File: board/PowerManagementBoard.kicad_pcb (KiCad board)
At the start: 2 copper layers, 167.9 x 115.3 mm, 162 parts, among them IC1 ACS37010LLZATR-030B3, IC2 ACS37010LLZATR-030B3, IC3 ACS37010LLZATR-030B3, IC4 ACS37010LLZATR-030B3, IC6 ACS37010LLZATR-030B3, J1 RJ45_LED_Shielded, J10 768250002, J11 768250002, J12 768250002, J13 768250002, J14 768250002, J15 768250002, J16 768250002, J17 768250002, J18 768250002, J2 SS-73100-082, J3 SS-73100-082, J5 768250002, J6 768250002, J7 768250002, J8 768250002, J9 768250002, Q1 BSS138, Q2 IPB180N10S4-02, Q3 Si4162DY, Q4 IPB180N10S4-02, Q5 Si4162DY, Q6 Si4162DY, Q7 Si4162DY, Q8 Si4162DY, Q9 IPB180N10S4-02, U1 LT1910, U10 ACS72981LLRATR-100U3, U11 LT1910, U12 LT1910, U13 LT1910, U14 LT1910, U15 Teensy4.1_DEV-16771, U16 OKI-78SR-3.3_1.5-W36H-C, U17 OKI-78SR-5_1.5-W36H-C, U19 LT1910, U2 LM5050MK-1_NOPB, U3 LM5050MK-1_NOPB, U4 Opamp_Dual, U5 Opamp_Dual, U6 Opamp_Dual

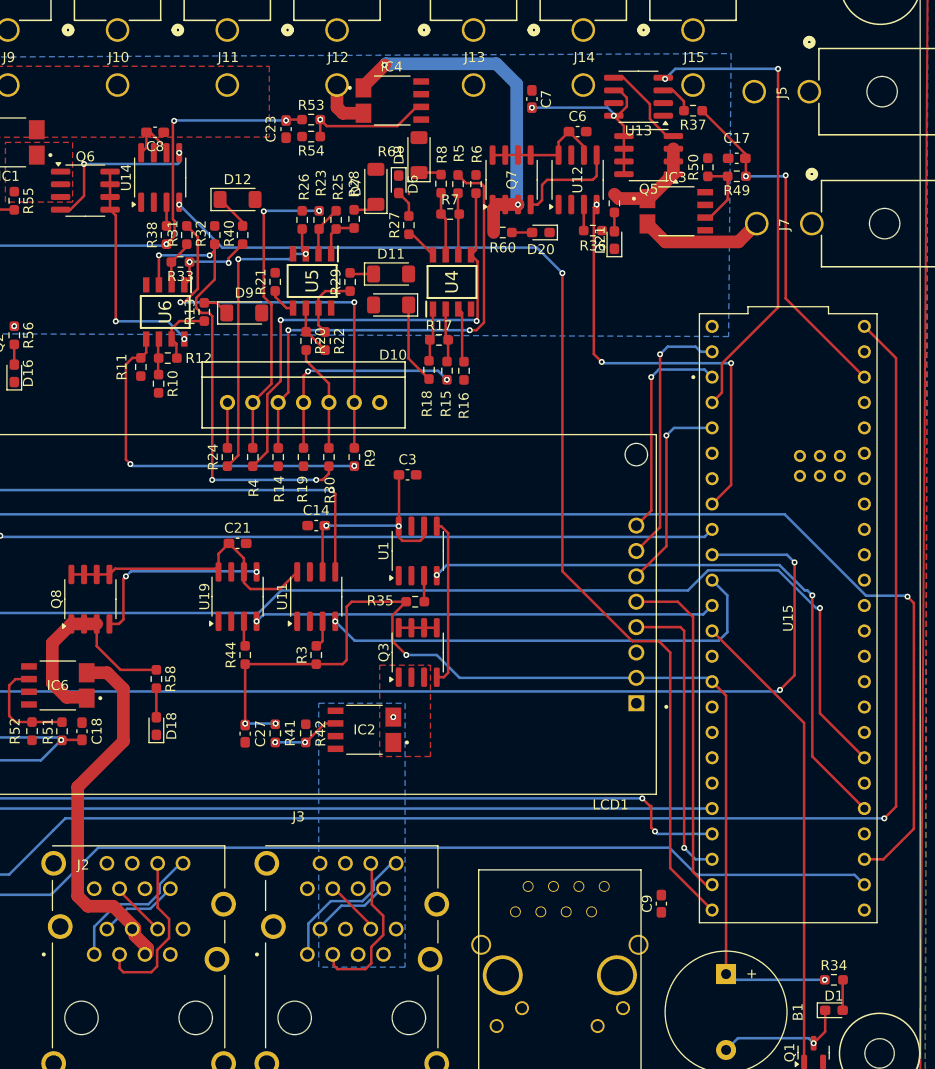
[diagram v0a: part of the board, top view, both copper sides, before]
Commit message: add more traces
seems to be just 24V connections left
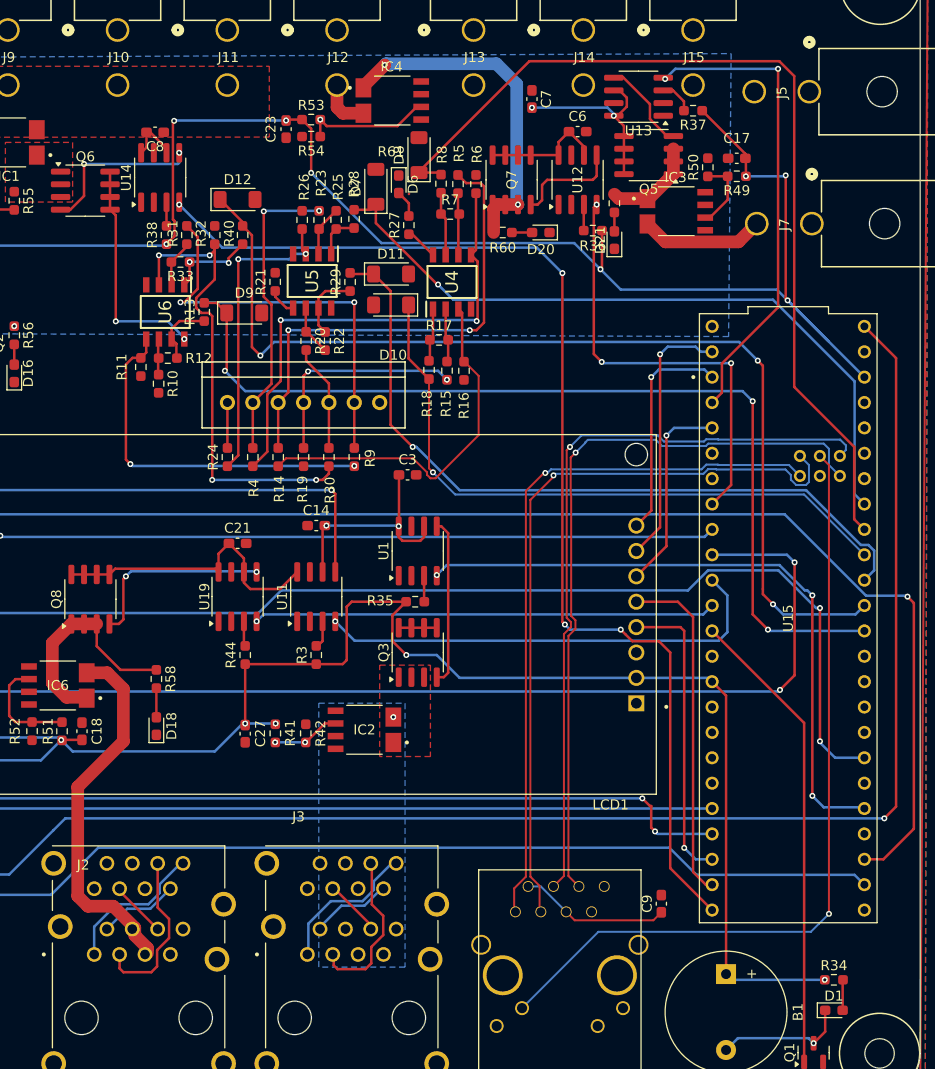
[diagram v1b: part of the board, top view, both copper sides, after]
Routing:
- net /TeensyandEthernetCircuit/CellSense2: track 3.58 -> 103.4 mm, vias 0 -> 3
- net /TeensyandEthernetCircuit/CellSense1: track 2.67 -> 95.8 mm, vias 0 -> 3
- net /TeensyandEthernetCircuit/CellSense5: track 2.29 -> 93.4 mm
- net +3V3: track 340.9 -> 429.4 mm, vias 14 -> 17
- net /TeensyandEthernetCircuit/LED: track 0.00 -> 80.8 mm, vias 0 -> 1
- net /TeensyandEthernetCircuit/RX+: track 0.00 -> 75.0 mm, vias 0 -> 1
- net /TeensyandEthernetCircuit/TX-: track 0.00 -> 74.9 mm, vias 0 -> 1
- net /TeensyandEthernetCircuit/RX-: track 0.00 -> 74.3 mm, vias 0 -> 1
- net /TeensyandEthernetCircuit/CellSense3: track 2.40 -> 75.2 mm, vias 0 -> 1
- net /TeensyandEthernetCircuit/TX+: track 0.00 -> 71.7 mm, vias 0 -> 1
- net /TeensyandEthernetCircuit/CellSense6: track 2.41 -> 71.5 mm, vias 0 -> 1
- net /TeensyandEthernetCircuit/CellSense4: track 8.26 -> 64.4 mm, vias 0 -> 1
- net Net-(U4A-+): track 5.50 -> 36.6 mm
- net Net-(C9-Pad1): track 0.00 -> 15.1 mm
- net /Switching Circuit/LC_EN: track 112.7 -> 115.7 mm, vias 2 -> 4
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
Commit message: Changes before layout review
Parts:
- added D17: GRN, LED_SMD:LED_0603_1608Metric_Pad1.05x0.95mm_HandSolder, F.Cu at (152.8, 109.7)
- added R57: 6.8k, Resistor_SMD:R_0603_1608Metric_Pad0.98x0.95mm_HandSolder, F.Cu at (152.7, 112.3)
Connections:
- net /Current-Sensinator/m5Vout renamed /TeensyandEthernetCircuit/CSensem5
- IC1 pad 7: (no net) -> /Current-Sensinator/LCVout
- IC1 pad 8: (no net) -> +3V3
- IC2 pad 7: (no net) -> /Current-Sensinator/m2Vout
- IC2 pad 8: (no net) -> +3V3
- IC3 pad 7: (no net) -> /Current-Sensinator/NSVout
- IC3 pad 8: (no net) -> +3V3
- IC4 pad 7: (no net) -> /Current-Sensinator/AUXVout
- IC4 pad 8: (no net) -> +3V3
- IC6 pad 7: (no net) -> /Current-Sensinator/m9Vout
- IC6 pad 8: (no net) -> +3V3
- U15 pad 36: /Switching Circuit/M5_EN -> unconnected-(U15-CS2-Pad36)
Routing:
- net +24V: track 167.1 -> 358.5 mm, vias 8 -> 17
- net /Current-Sensinator/LCVout: track 0.00 -> 183.2 mm, vias 0 -> 3
- net /Current-Sensinator/m9out: track 37.6 -> 152.8 mm, vias 0 -> 3
- net /Current-Sensinator/AUXVout: track 0.00 -> 87.3 mm, vias 0 -> 4
- net /Current-Sensinator/m9Vout: track 0.00 -> 71.1 mm, vias 0 -> 1
- net /Current-Sensinator/NSVout: track 0.00 -> 59.9 mm
- net /Current-Sensinator/m2Vout: track 0.00 -> 54.9 mm, vias 0 -> 1
- net +3V3: track 429.4 -> 475.6 mm, vias 17 -> 19
- net /Current-Sensinator/m2out: track 0.00 -> 25.1 mm
- net Net-(U5B-+): track 2.84 -> 19.2 mm
- net GND: track 0.07 -> 9.45 mm
- net Net-(D17-A): track 0.00 -> 2.55 mm
- net /Current-Sensinator/m9in: track 22.7 -> 21.6 mm
- net Net-(U4A-+): track 36.6 -> 36.8 mm, vias 0 -> 2
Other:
- board size 167.9 x 115.3 mm -> 167.6 x 115.1 mm

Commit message: experimented with layout
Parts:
- removed the C13 at (75.0, 122.2)
- removed the C4 at (76.2, 97.3)
- removed R41, R42, R43, R46, R49, R50, R51, R52, R53, R54: 10k, Resistor_SMD:R_0603_1608Metric_Pad0.98x0.95mm_HandSolder
- moved J7 100.4 mm to (108.7, 117.7), turned to 0 degrees
- moved J5 98.1 mm to (122.8, 117.7), turned to 0 degrees
- moved D1 88.9 mm to (164.8, 54.4), turned to 180 degrees
- moved D6 88.7 mm to (77.7, 108.2), turned to 180 degrees
- moved Q1 88.7 mm to (164.8, 58.2)
- moved R34 86.4 mm to (161.0, 55.4), turned to 90 degrees
- moved R27 86.1 mm to (77.7, 106.2), turned to 180 degrees
- moved B1 77.8 mm to (177.8, 57.4), turned to 180 degrees
- moved Q5 74.5 mm to (112.0, 93.7)
- moved D21 74.3 mm to (111.3, 105.7)
- moved R61 74.1 mm to (111.3, 101.6)
- moved C17 73.8 mm to (124.1, 97.5), turned to 0 degrees
- moved C7 72.8 mm to (110.2, 97.8), turned to 180 degrees
- moved IC3 72.5 mm to (117.3, 99.6)
- moved U13 70.4 mm to (120.7, 93.7)
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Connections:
- net Net-(D14-K) renamed /Current Protection/Batt_to_CS
- net Net-(D2-K) renamed /Current Protection/Batt2
- net Net-(D4-K) renamed /Current Protection/Batt1
- IC1 pad 6: Net-(IC1-VREF) -> unconnected-(IC1-VREF-Pad6)
- IC2 pad 6: Net-(IC2-VREF) -> unconnected-(IC2-VREF-Pad6)
- IC3 pad 6: Net-(IC3-VREF) -> unconnected-(IC3-VREF-Pad6)
- IC4 pad 6: Net-(IC4-VREF) -> unconnected-(IC4-VREF-Pad6)
- IC6 pad 6: Net-(IC6-VREF) -> unconnected-(IC6-VREF-Pad6)
- R10 pad 1: Net-(U6B--) -> Net-(U6A--)
- R11 pad 1: Net-(U6B-+) -> Net-(U6A-+)
- R12 pad 2: Net-(U6B--) -> Net-(U6A--)
- R14 pad 1: Net-(U4A-+) -> Net-(U5B-+)
- R15 pad 1: Net-(U4A--) -> Net-(U5B--)
- R16 pad 1: Net-(U4A-+) -> Net-(U5B-+)
- R17 pad 2: Net-(U4A--) -> Net-(U5B--)
- R19 pad 1: Net-(U5B-+) -> Net-(U5A-+)
- R20 pad 1: Net-(U5B--) -> Net-(U5A--)
- R21 pad 1: Net-(U5B-+) -> Net-(U5A-+)
- R22 pad 2: Net-(U5B--) -> Net-(U5A--)
- R23 pad 1: Net-(U5A--) -> Net-(U4B--)
- R24 pad 1: Net-(U5A-+) -> Net-(U4B-+)
- R25 pad 2: Net-(U5A--) -> Net-(U4B--)
- R26 pad 1: Net-(U5A-+) -> Net-(U4B-+)
- R30 pad 1: Net-(U6A-+) -> Net-(U6B-+)
- R31 pad 1: Net-(U6A--) -> Net-(U6B--)
- R32 pad 1: Net-(U6A-+) -> Net-(U6B-+)
- R33 pad 2: Net-(U6A--) -> Net-(U6B--)
- R4 pad 1: Net-(U4B-+) -> Net-(U4A-+)
- R5 pad 1: Net-(U4B--) -> Net-(U4A--)
- R6 pad 1: Net-(U4B-+) -> Net-(U4A-+)
- R7 pad 2: Net-(U4B--) -> Net-(U4A--)
- R9 pad 1: Net-(U6B-+) -> Net-(U6A-+)
- U15 pad 10: /Switching Circuit/M9_EN -> unconnected-(U15-CS1-Pad10)
- U15 pad 27: /TeensyandEthernetCircuit/CSensem5 -> unconnected-(U15-A13-Pad27)
- U15 pad 3.3V_1: +3V3 -> unconnected-(U15-3.3V-Pad3.3V_1)
- U15 pad 3.3V_2: +3V3 -> unconnected-(U15-3.3V-Pad3.3V_1)_1
- U15 pad 36: unconnected-(U15-CS2-Pad36) -> /Switching Circuit/M9_EN
- U4 pad 1: Net-(R17-Pad1) -> Net-(R7-Pad1)
- U4 pad 7: Net-(R7-Pad1) -> Net-(R25-Pad1)
- U5 pad 1: Net-(R25-Pad1) -> Net-(R22-Pad1)
- U5 pad 7: Net-(R22-Pad1) -> Net-(R17-Pad1)
- U6 pad 1: Net-(R33-Pad1) -> Net-(R12-Pad1)
- U6 pad 7: Net-(R12-Pad1) -> Net-(R33-Pad1)
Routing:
- net +3V3: track 475.6 -> 0.00 mm, vias 19 -> 0
- net +24V: track 358.5 -> 146.4 mm, vias 17 -> 1
- net +5V: track 183.5 -> 0.00 mm, vias 1 -> 0
- net /Current-Sensinator/LCVout: track 183.2 -> 0.00 mm, vias 3 -> 0
- net /LCD/D6: track 153.2 -> 0.00 mm, vias 1 -> 0
- net /Current-Sensinator/m9out: track 152.8 -> 0.00 mm, vias 3 -> 0
- net /LCD/D7: track 137.8 -> 0.00 mm, vias 1 -> 0
- net /Current Protection/BattVout: track 135.7 -> 0.00 mm, vias 4 -> 0
- net /Switching Circuit/LC_EN: track 115.7 -> 0.00 mm, vias 4 -> 0
- net /LCD/D3: track 111.9 -> 0.00 mm, vias 2 -> 0
- net /TeensyandEthernetCircuit/CellSense2: track 103.4 -> 0.00 mm, vias 3 -> 0
- net /LCD/D2: track 100.0 -> 0.00 mm, vias 2 -> 0
- net /LCD/D5: track 99.4 -> 0.00 mm, vias 3 -> 0
- net /TeensyandEthernetCircuit/CellSense1: track 95.8 -> 0.00 mm, vias 3 -> 0
- net /LCD/D4: track 95.4 -> 0.00 mm, vias 1 -> 0
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- added copper zone on B.Cu, net +24V
- added copper zone on F.Cu, net /Anderson/AUX
- removed copper zone on F.Cu, net /Current-Sensinator/m2in
- removed copper zone on B.Cu, net /Current-Sensinator/m2out
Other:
- board size 167.6 x 115.1 mm -> 162.3 x 99.6 mm

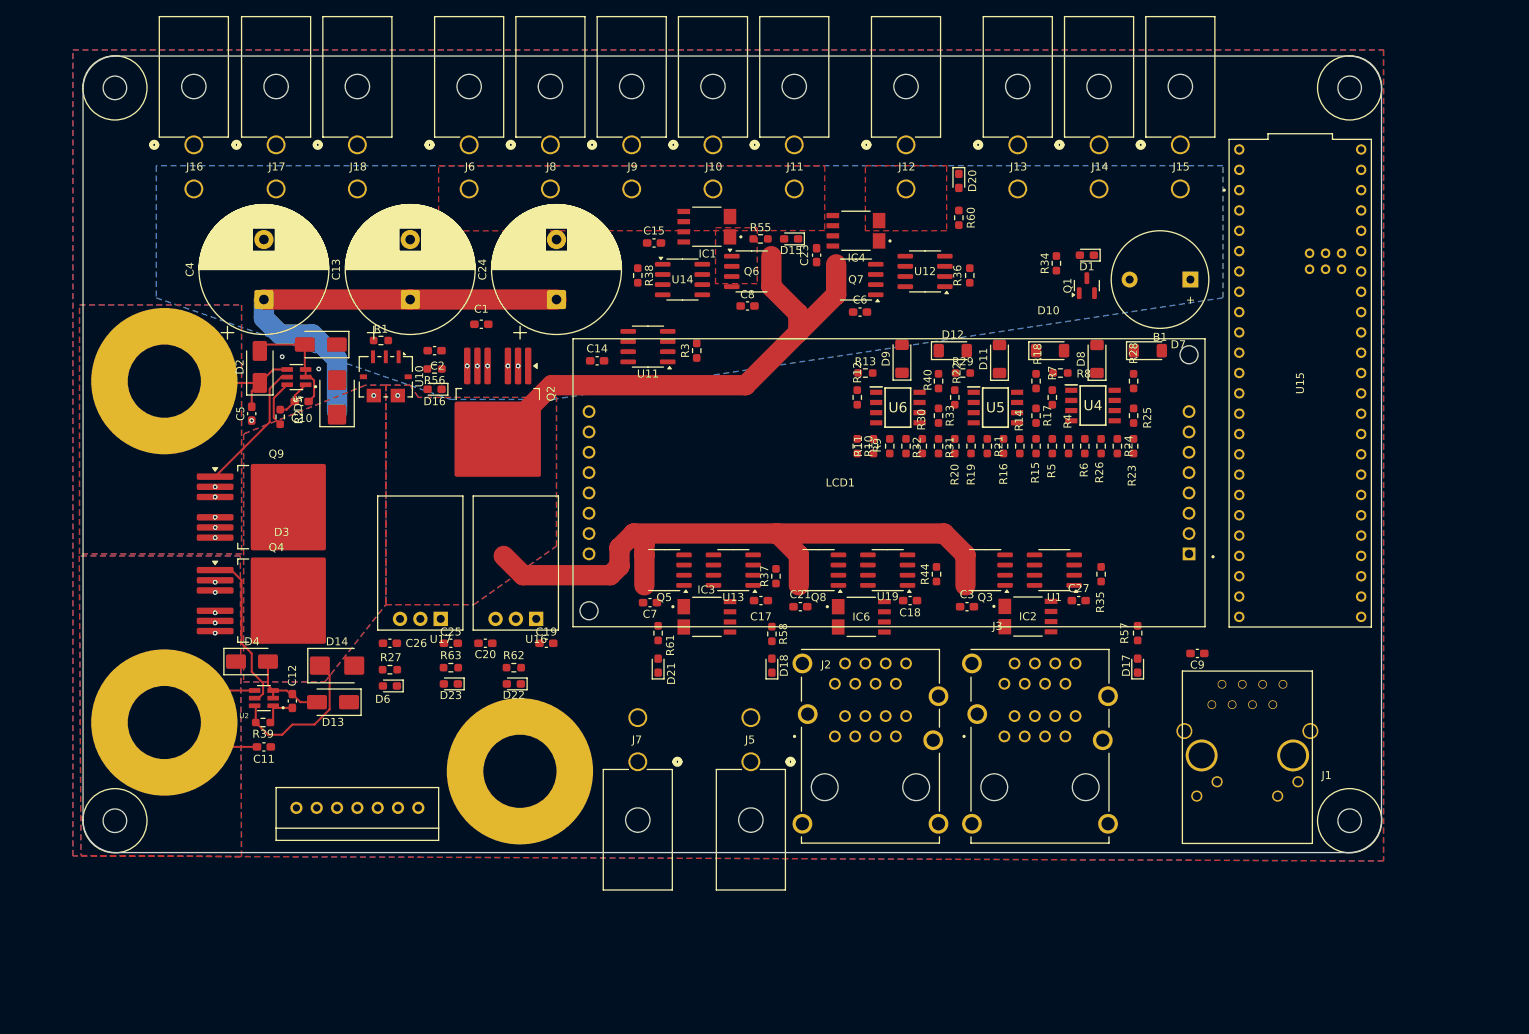
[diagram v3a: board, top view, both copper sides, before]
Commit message: move ground ring terminal
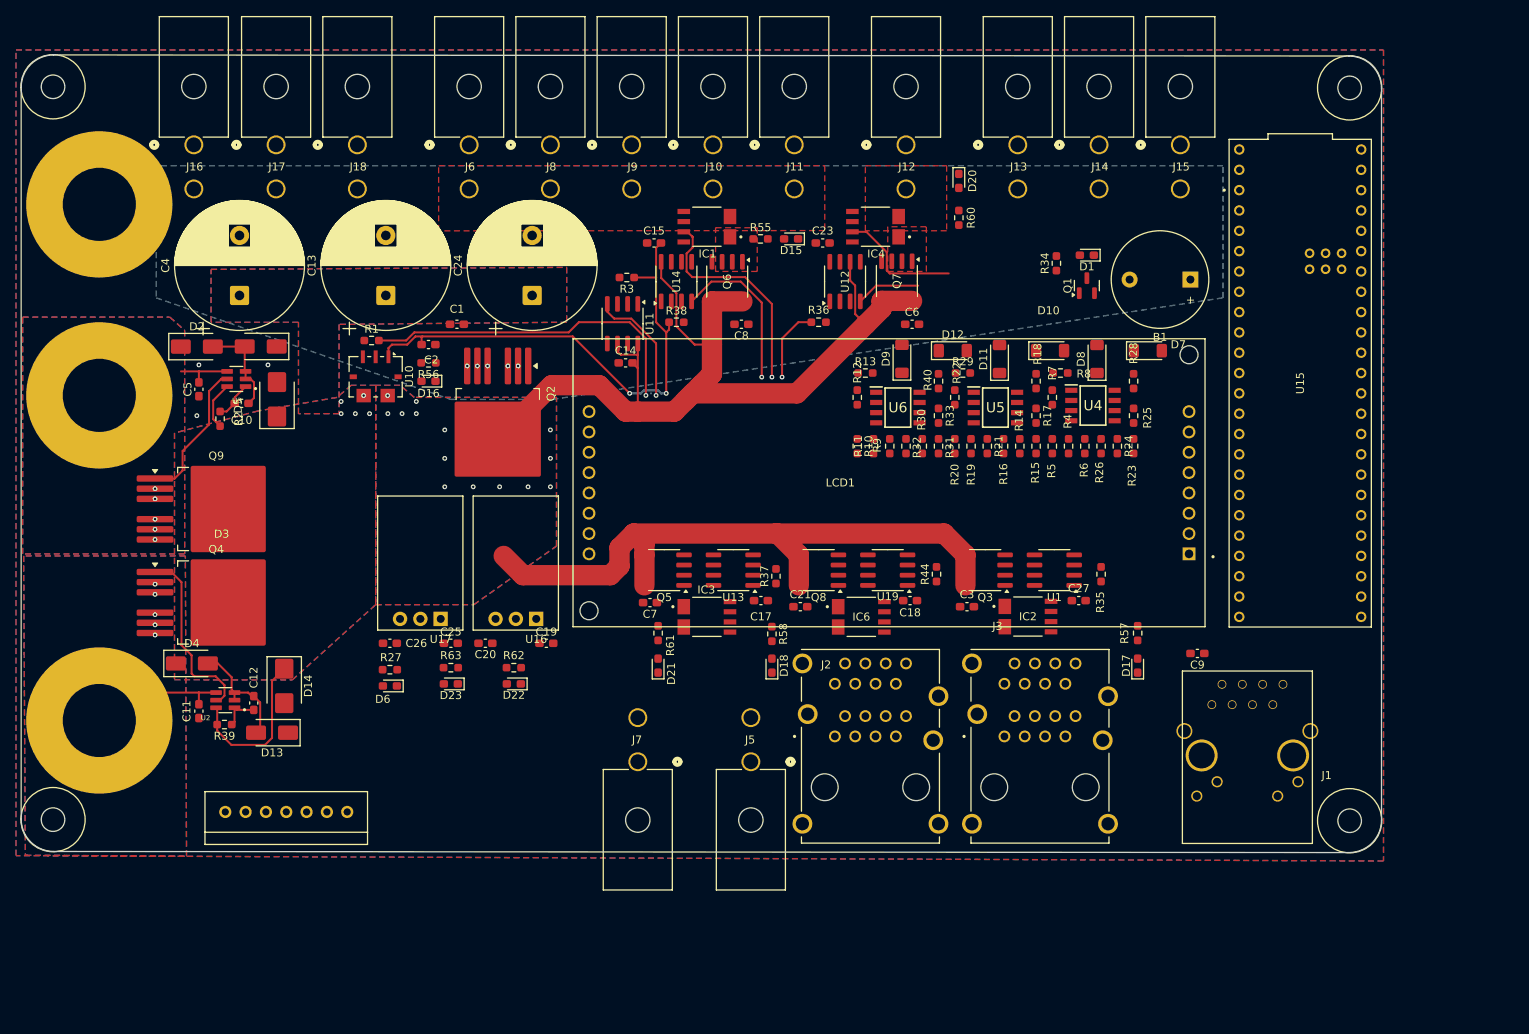
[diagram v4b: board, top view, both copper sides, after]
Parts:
- moved V2 88.2 mm to (41.4, 48.0)
- moved R36 19.8 mm to (131.3, 62.7), turned to 0 degrees
- moved R3 12.6 mm to (107.3, 57.1), turned to 180 degrees
- moved U12 10.1 mm to (134.6, 57.7), turned to 90 degrees
- moved C11 9.28 mm to (53.8, 111.4), turned to -90 degrees
- moved Conn1 8.90 mm to (72.4, 124.0)
- moved D13 8.52 mm to (63.0, 114.0)
- moved V3 8.32 mm to (41.4, 71.9)
- moved D2 8.27 mm to (53.6, 65.8), turned to 0 degrees
- moved V1 8.13 mm to (41.4, 112.5)
- moved H2 7.74 mm to (39.6, 120.9)
- moved H3 7.74 mm to (39.6, 37.3)
- moved R38 7.58 mm to (113.5, 62.7), turned to 0 degrees
- moved D4 7.51 mm to (53.0, 105.4)
- moved D5 7.51 mm to (63.6, 72.4)
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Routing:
- net +3V3: track 0.00 -> 73.8 mm, vias 0 -> 3
- net /Current Protection/Batt_to_CS: track 82.1 -> 26.2 mm, vias 1 -> 5
- net +24V: track 146.4 -> 197.8 mm, vias 1 -> 14
- net /Current Protection/BattVout: track 0.00 -> 42.3 mm, vias 0 -> 1
- net /Current-Sensinator/LCVout: track 0.00 -> 27.5 mm, vias 0 -> 1
- net /Switching Circuit/LC_EN: track 0.00 -> 20.2 mm, vias 0 -> 1
- net /Current Protection/Batt1: track 25.8 -> 8.75 mm
- net /Current-Sensinator/AUXVout: track 0.00 -> 15.5 mm
- net /Switching Circuit/Motor_EN: track 0.00 -> 15.2 mm, vias 0 -> 1
- net /Current Protection/Batt2: track 19.5 -> 7.46 mm
- net /Switching Circuit/AUX_EN: track 0.00 -> 8.05 mm
- net Net-(D13-A): track 10.9 -> 14.4 mm
- net Net-(Q4-G): track 20.4 -> 23.1 mm
- net Net-(D2-A): track 14.2 -> 12.2 mm
- net Net-(Q9-G): track 16.6 -> 18.0 mm
- added copper zone on F.Cu, net /Current-Sensinator/AUXin
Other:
- board size 162.3 x 99.6 mm -> 170 x 99.7 mm
